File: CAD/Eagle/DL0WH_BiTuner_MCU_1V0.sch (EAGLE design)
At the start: 112 parts, among them Q0321 ABS07-32.768KHZ, U0101 STM32L476RXT_64PIN_LDO, U0521 PCAL6416APW, U2401 LM53603-Q1, U9001 TPS62051, U9401 MC33996, U9501 MC33996, U9601 MC33996, U9801 MAX232_SOIC16, U9901 MAX232_SOIC16, X2411 WIRE-TO-BOARD_5MM08_1X02, X3201 MOLEX 105017-0001, X3301 SMA_SMT_AMPHENOL-901-143, X3311 SAMTEC SMA-J-P-H-RA-TH1, X9851 WIRE-TO-BOARD_5MM08_1X02, X9852 WIRE-TO-BOARD_5MM08_1X02, X9853 WIRE-TO-BOARD_5MM08_1X02, X9951 WIRE-TO-BOARD_5MM08_1X02, X9952 WIRE-TO-BOARD_5MM08_1X02, X9953 WIRE-TO-BOARD_5MM08_1X02

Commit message: HW_1V0 - CAD/Eagle - I2C port expander not needed and removed
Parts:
- removed C0521: 100nF, df4iah_rcl:C-EUC0402
- removed R0521: 100kR, df4iah_rcl:R-EU_R0402
- removed U0521: PCAL6416APW, df4iah_dataconvertion:PCAL6416APW
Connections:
- removed net PEXPA_P0_0_R: U0521.P0_0
- removed net PEXPA_P0_1_R: U0521.P0_1
- removed net PEXPA_P0_2_R: U0521.P0_2
- removed net PEXPA_P0_3_R: U0521.P0_3
- removed net PEXPA_P0_4_R: U0521.P0_4
- removed net PEXPA_P0_5_R: U0521.P0_5
- removed net PEXPA_P0_6_R: U0521.P0_6
- removed net PEXPA_P0_7_R: U0521.P0_7
- removed net PEXPA_P1_0_R: U0521.P1_0
- removed net PEXPA_P1_1_R: U0521.P1_1
- removed net PEXPA_P1_2_R: U0521.P1_2
- removed net PEXPA_P1_3_R: U0521.P1_3
- removed net PEXPA_P1_4_R: U0521.P1_4
- removed net PEXPA_P1_5_R: U0521.P1_5
- removed net PEXPA_P1_6_R: U0521.P1_6
- removed net PEXPA_P1_7_R: U0521.P1_7
- removed net PEXPA_RESET: R0521.1, U0521.!RESET
- net +3V3: no longer C0521.1, R0521.2, U0521.VDD_I2C, U0521.VDD_P
- net GND: no longer C0521.2, U0521.ADDR, U0521.VSS
- net MCU_I2C1_SCL: no longer U0521.SCL
- net MCU_I2C1_SDA: no longer U0521.SDA
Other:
- note added: "Addr Device"
- note removed: "Addr Device 0x20/0x21 I2C Port Expander A/B 0x3D LCD access"
- note removed: "I2C1 Port Expander"
- note removed: "I2C1 Port Expander I2C1 addr: 0x20"
- note removed: "Iq=6.5uA"
- note removed: "out"
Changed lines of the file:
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@@
 <part name="GND3661" library="df4iah_supply" deviceset="GND" device=""/>
 <part name="L0411" library="df4iah_rcl" deviceset="L-EU" device="L0603" value="10uH"/>
-<part name="GND0521" library="df4iah_supply" deviceset="GND" device=""/>
-<part name="C0521" library="df4iah_rcl" deviceset="C-EU" device="C0402" value="100nF"/>
-<part name="FRAME_05" library="df4iah_frame" deviceset="A4L-LOC" device="" value="Holes"/>
-<part name="U0521" library="df4iah_dataconvertion" deviceset="PCAL6416A" device="PW"/>
-<part name="R0521" library="df4iah_rcl" deviceset="R-EU_" device="R0402" value="100kR"/>
 <part name="FRAME_24" library="df4iah_frame" deviceset="A4L-LOC" device="" value="Holes"/>
 <part name="L2411" library="df4iah_rcl" deviceset="L-EU" device="6.00X6.00MM" value="2.2uH"/>
@@
 <plain>
 <text x="134.62" y="137.16" size="2.54" layer="97" ratio="15">Addr        Device
-0x20/0x21   I2C Port Expander A/B
-0x3D        LCD access
 </text>
 <text x="22.86" y="162.56" size="2.54" layer="97" ratio="15">I2C1 Termination</text>
@@
 </segment>
 </net>
-</nets>
-</sheet>
-<sheet>
-<description>I2C1 Port Expander</description>
-<plain>
-<text x="22.86" y="162.56" size="2.54" layer="97" ratio="15">I2C1 Port Expander
-I2C1 addr: 0x20</text>
-<text x="165.1" y="15.24" size="2.54" layer="97" ratio="15">I2C1 Port Expander</text>
-<text x="106.68" y="132.08" size="1.778" layer="97">Iq=6.5uA</text>
-<text x="135.636" y="126.238" size="1.778" layer="97">out</text>
-<text x="135.636" y="121.158" size="1.778" layer="97">out</text>
-<text x="135.636" y="116.078" size="1.778" layer="97">out</text>
-<text x="135.636" y="110.998" size="1.778" layer="97">out</text>
-<text x="135.636" y="105.918" size="1.778" layer="97">out</text>
-<text x="135.636" y="100.838" size="1.778" layer="97">out</text>
-<text x="135.636" y="95.758" size="1.778" layer="97">out</text>
-<text x="135.636" y="90.678" size="1.778" layer="97">out</text>
-<text x="135.636" y="44.958" size="1.778" layer="97">out</text>
-<text x="135.636" y="50.038" size="1.778" layer="97">out</text>
-<text x="135.636" y="55.118" size="1.778" layer="97">out</text>
-<text x="135.636" y="60.198" size="1.778" layer="97">out</text>
-<text x="135.636" y="65.278" size="1.778" layer="97">out</text>
-<text x="135.636" y="70.358" size="1.778" layer="97">out</text>
-<text x="135.636" y="75.438" size="1.778" layer="97">out</text>
-<text x="135.636" y="80.518" size="1.778" layer="97">out</text>
-</plain>
-<instances>
-<instance part="FRAME_05" gate="G$1" x="0" y="0"/>
-<instance part="GND0521" gate="1" x="104.14" y="71.12"/>
-<instance part="C0521" gate="G$1" x="104.14" y="101.6"/>
-<instance part="U0521" gate="G$1" x="132.08" y="86.36"/>
-<instance part="R0521" gate="G$1" x="93.98" y="93.98" smashed="yes" rot="R90">
-<attribute name="NAME" x="92.4814" y="90.17" size="1.778" layer="95" rot="R90"/>
-<attribute name="VALUE" x="97.282" y="90.17" size="1.778" layer="96" rot="R90"/>
-</instance>
-</instances>
-<busses>
-</busses>
-<nets>
-<net name="MCU_I2C1_SCL" class="0">
-<segment>
-<wire x1="109.22" y1="66.04" x2="88.9" y2="66.04" width="0.1524" layer="91"/>
-<label x="88.9" y="66.04" size="1.778" layer="95" rot="R180" xref="yes"/>
-<pinref part="U0521" gate="G$1" pin="SCL"/>
-</segment>
-</net>
-<net name="MCU_I2C1_SDA" class="0">
-<segment>
-<wire x1="109.22" y1="60.96" x2="88.9" y2="60.96" width="0.1524" layer="91"/>
-<label x="88.9" y="60.96" size="1.778" layer="95" rot="R180" xref="yes"/>
-<pinref part="U0521" gate="G$1" pin="SDA"/>
-</segment>
-</net>
-<net name="+3V3" class="0">
-<segment>
-<wire x1="104.14" y1="104.14" x2="104.14" y2="106.68" width="0.1524" layer="91"/>
-<label x="104.14" y="134.62" size="1.778" layer="95" rot="R90" xref="yes"/>
-<pinref part="U0521" gate="G$1" pin="VDD_I2C"/>
-<wire x1="104.14" y1="106.68" x2="104.14" y2="121.92" width="0.1524" layer="91"/>
-<wire x1="104.14" y1="121.92" x2="104.14" y2="127" width="0.1524" layer="91"/>
-<wire x1="104.14" y1="127" x2="104.14" y2="134.62" width="0.1524" layer="91"/>
-<wire x1="104.14" y1="121.92" x2="109.22" y2="121.92" width="0.1524" layer="91"/>
-<junction x="104.14" y="121.92"/>
-<pinref part="U0521" gate="G$1" pin="VDD_P"/>
-<wire x1="104.14" y1="127" x2="109.22" y2="127" width="0.1524" layer="91"/>
-<junction x="104.14" y="127"/>
-<pinref part="R0521" gate="G$1" pin="2"/>
-<wire x1="93.98" y1="106.68" x2="93.98" y2="99.06" width="0.1524" layer="91"/>
-<wire x1="104.14" y1="106.68" x2="93.98" y2="106.68" width="0.1524" layer="91"/>
-<junction x="104.14" y="106.68"/>
-<pinref part="C0521" gate="G$1" pin="1"/>
-</segment>
-</net>
-<net name="PEXPA_P1_7_R" class="0">
-<segment>
-<wire x1="154.94" y1="45.72" x2="177.8" y2="45.72" width="0.1524" layer="91"/>
-<label x="177.8" y="45.72" size="1.778" layer="95" xref="yes"/>
-<pinref part="U0521" gate="G$1" pin="P1_7"/>
-</segment>
-</net>
-<net name="PEXPA_P0_1_R" class="0">
-<segment>
-<wire x1="154.94" y1="121.92" x2="177.8" y2="121.92" width="0.1524" layer="91"/>
-<label x="177.8" y="121.92" size="1.778" layer="95" xref="yes"/>
-<pinref part="U0521" gate="G$1" pin="P0_1"/>
-</segment>
-</net>
-<net name="PEXPA_P0_2_R" class="0">
-<segment>
-<wire x1="154.94" y1="116.84" x2="177.8" y2="116.84" width="0.1524" layer="91"/>
-<label x="177.8" y="116.84" size="1.778" layer="95" xref="yes"/>
-<pinref part="U0521" gate="G$1" pin="P0_2"/>
-</segment>
-</net>
-<net name="PEXPA_P0_3_R" class="0">
-<segment>
-<wire x1="154.94" y1="111.76" x2="177.8" y2="111.76" width="0.1524" layer="91"/>
-<label x="177.8" y="111.76" size="1.778" layer="95" xref="yes"/>
-<pinref part="U0521" gate="G$1" pin="P0_3"/>
-</segment>
-</net>
-<net name="PEXPA_P0_4_R" class="0">
-<segment>
-<wire x1="154.94" y1="106.68" x2="177.8" y2="106.68" width="0.1524" layer="91"/>
-<label x="177.8" y="106.68" size="1.778" layer="95" xref="yes"/>
-<pinref part="U0521" gate="G$1" pin="P0_4"/>
-</segment>
-</net>
-<net name="PEXPA_P0_5_R" class="0">
-<segment>
-<wire x1="154.94" y1="101.6" x2="177.8" y2="101.6" width="0.1524" layer="91"/>
-<label x="177.8" y="101.6" size="1.778" layer="95" xref="yes"/>
-<pinref part="U0521" gate="G$1" pin="P0_5"/>
-</segment>
-</net>
-<net name="PEXPA_P0_6_R" class="0">
-<segment>
-<wire x1="154.94" y1="96.52" x2="177.8" y2="96.52" width="0.1524" layer="91"/>
-<label x="177.8" y="96.52" size="1.778" layer="95" xref="yes"/>
-<pinref part="U0521" gate="G$1" pin="P0_6"/>
-</segment>
-</net>
-<net name="PEXPA_P0_7_R" class="0">
-<segment>
-<wire x1="154.94" y1="91.44" x2="177.8" y2="91.44" width="0.1524" layer="91"/>
-<label x="177.8" y="91.44" size="1.778" layer="95" xref="yes"/>
-<pinref part="U0521" gate="G$1" pin="P0_7"/>
-</segment>
-</net>
-<net name="PEXPA_P1_0_R" class="0">
-<segment>
-<wire x1="154.94" y1="81.28" x2="177.8" y2="81.28" width="0.1524" layer="91"/>
-<label x="177.8" y="81.28" size="1.778" layer="95" xref="yes"/>
-<pinref part="U0521" gate="G$1" pin="P1_0"/>
-</segment>
-</net>
-<net name="PEXPA_P1_1_R" class="0">
-<segment>
-<wire x1="154.94" y1="76.2" x2="177.8" y2="76.2" width="0.1524" layer="91"/>
-<label x="177.8" y="76.2" size="1.778" layer="95" xref="yes"/>
-<pinref part="U0521" gate="G$1" pin="P1_1"/>
-</segment>
-</net>
-<net name="PEXPA_P1_2_R" class="0">
-<segment>
-<wire x1="154.94" y1="71.12" x2="177.8" y2="71.12" width="0.1524" layer="91"/>
-<label x="177.8" y="71.12" size="1.778" layer="95" xref="yes"/>
-<pinref part="U0521" gate="G$1" pin="P1_2"/>
-</segment>
-</net>
-<net name="PEXPA_P1_3_R" class="0">
-<segment>
-<wire x1="154.94" y1="66.04" x2="177.8" y2="66.04" width="0.1524" layer="91"/>
-<label x="177.8" y="66.04" size="1.778" layer="95" xref="yes"/>
-<pinref part="U0521" gate="G$1" pin="P1_3"/>
-</segment>
-</net>
-<net name="PEXPA_P1_4_R" class="0">
-<segment>
-<wire x1="154.94" y1="60.96" x2="177.8" y2="60.96" width="0.1524" layer="91"/>
-<label x="177.8" y="60.96" size="1.778" layer="95" xref="yes"/>
-<pinref part="U0521" gate="G$1" pin="P1_4"/>
-</segment>
-</net>
-<net name="PEXPA_P1_5_R" class="0">
-<segment>
-<wire x1="154.94" y1="55.88" x2="177.8" y2="55.88" width="0.1524" layer="91"/>
-<label x="177.8" y="55.88" size="1.778" layer="95" xref="yes"/>
-<pinref part="U0521" gate="G$1" pin="P1_5"/>
-</segment>
-</net>
-<net name="PEXPA_P1_6_R" class="0">
-<segment>
-<wire x1="154.94" y1="50.8" x2="177.8" y2="50.8" width="0.1524" layer="91"/>
-<label x="177.8" y="50.8" size="1.778" layer="95" xref="yes"/>
-<pinref part="U0521" gate="G$1" pin="P1_6"/>
-</segment>
-</net>
-<net name="GND" class="0">
-<segment>
-<wire x1="109.22" y1="81.28" x2="104.14" y2="81.28" width="0.1524" layer="91"/>
-<wire x1="104.14" y1="81.28" x2="104.14" y2="91.44" width="0.1524" layer="91"/>
-<wire x1="104.14" y1="91.44" x2="109.22" y2="91.44" width="0.1524" layer="91"/>
-<pinref part="GND0521" gate="1" pin="GND"/>
-<wire x1="104.14" y1="73.66" x2="104.14" y2="81.28" width="0.1524" layer="91"/>
-<junction x="104.14" y="81.28"/>
-<pinref part="C0521" gate="G$1" pin="2"/>
-<wire x1="104.14" y1="91.44" x2="104.14" y2="96.52" width="0.1524" layer="91"/>
-<junction x="104.14" y="91.44"/>
-<pinref part="U0521" gate="G$1" pin="ADDR"/>
-<pinref part="U0521" gate="G$1" pin="VSS"/>
-</segment>
-</net>
-<net name="PEXPA_P0_0_R" class="0">
-<segment>
-<wire x1="154.94" y1="127" x2="177.8" y2="127" width="0.1524" layer="91"/>
-<label x="177.8" y="127" size="1.778" layer="95" xref="yes"/>
-<pinref part="U0521" gate="G$1" pin="P0_0"/>
-</segment>
-</net>
-<net name="PEXPA_RESET" class="0">
-<segment>
-<pinref part="R0521" gate="G$1" pin="1"/>
-<wire x1="93.98" y1="88.9" x2="93.98" y2="76.2" width="0.1524" layer="91"/>
-<wire x1="93.98" y1="76.2" x2="109.22" y2="76.2" width="0.1524" layer="91"/>
-<pinref part="U0521" gate="G$1" pin="!RESET"/>
-</segment>
-</net>

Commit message: HW_1V0 - CAD/Eagle - I2C port added
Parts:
- added C8901, C8902: 10nF, df4iah_rcl:C-EUC0603
- added C8911: (no value), df4iah_rcl:C-EUC0603
- added C8921: 100nF, df4iah_rcl:C-EUC0603
- added D8921, D8922: CMAD6001, df4iah_diode:D_SOD923
- added L8901, L8902: 10uH, df4iah_rcl:L-EUL0603
- added R8901, R8902: 1kR, df4iah_rcl:R-EU_R0603
- added R8903, R8904, R8923: 10kR, df4iah_rcl:R-EU_R0603
- added R8911, R8912, R8922: 47R, df4iah_rcl:R-EU_R0603
- added R8921: 1MR, df4iah_rcl:R-EU_R0603
- added U8911: TS5A23166, df4iah_sc-switches:TS5A23166
- added U8921: OPA354, df4iah_opamp:OPA354
- added X0601: (no value), df4iah_connector:HEADER-2X2
- L9011: device df4iah_rcl:L-EU8.00X8.00MM -> df4iah_rcl:L-EUL0603
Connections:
- removed net MCU_I2C1_SCL: R0612.1
- removed net MCU_I2C1_SDA: R0611.1
- removed net N$1: R9901.1
- removed net N$10: R9621.1
- removed net N$11: R9622.1
- removed net N$14: R9623.1
- removed net N$16: R9624.1
- removed net N$17: R9625.1
- removed net N$18: R9626.1
- removed net N$3: R9902.1
- removed net N$30: R9524.1
- removed net N$31: R9424.1
- removed net N$4: R9903.1
- removed net N$5: R9904.1
- removed net N$6: R9801.1
- removed net N$7: R9802.1
- removed net N$8: R9803.1
- removed net N$9: R9804.1
- removed net PA12PA11_N: X3201.J_D-
- removed net PA12PA11_P: X3201.J_D+
- removed net RM_BCK: X3311.1
- new net RM_REV: L8902.2, X3311.1
- new net SWR_IN_FWD: R8902.2, R8904.2, U8911.1
- new net SWR_IN_FWD_HI: C8901.1, L8901.1, R8904.1
- new net SWR_IN_REV: R8901.2, R8903.2, U8911.5
- new net SWR_IN_REV_HI: C8902.1, L8902.1, R8903.1
- new net SWR_OP_M: D8921.A, R8921.2, U8921.-IN
- new net SWR_OP_OUT: D8921.C, R8922.1, U8921.OUT
- new net SWR_SEL_FWD: R8911.2, U8911.7
- new net SWR_SEL_PWR: R8921.1, U8911.2, U8911.6
- new net SWR_SEL_REV: R8912.2, U8911.3
- net +3V3: now also C8911.1, C8921.1, R8923.1, U8911.8, U8921.V+
- net GND: now also C8901.2, C8902.2, C8911.2, C8921.2, D8922.C, R8901.1, R8902.1, U8911.4, U8921.+IN, U8921.V-, X0601.2, X0601.4
- net PA0: now also R9901.1
- net PA1: now also R9902.1
- net PA11: now also X3201.J_D-
- net PA12: now also X3201.J_D+
- net PA15: now also R9903.1
- net PA3: now also R8912.1
- net PA5: now also R9621.1
- net PA6: now also R9622.1
- net PA7: now also R9623.1
- net PB0: now also R9624.1
- net PB1: now also R9524.1
- net PB10: now also R9802.1
- net PB11: now also R9626.1
- net PB12: now also R9803.1
- net PB13: now also R9804.1
- net PB2: now also R9424.1
- net PB6: now also R0612.1, X0601.1
- net PB7: now also R9904.1
- net PB9: now also R0611.1, X0601.3
- net PC0: now also R8922.2
- net PC1: now also R9801.1
- net PC2: now also D8922.A, R8923.2
- net PC3: now also R8911.1
- net PC4: now also R9625.1
- net RM_FWD: now also L8901.2
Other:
- note added: "Logarithmic Amp"
- note added: "MCU_I2C1_SCL"
- note added: "MCU_I2C1_SDA"
- note added: "PMIC 12V --> 5V0"
- note added: "SMA direct. coupler FWD"
- note added: "SMA direct. coupler REV"
- note added: "SWR metering"
- note added: "SWR_ADC"
- note added: "SWR_TEMP"
- note added: "Switch"
- note added: "WE PD 744 777 10 8.00mm x 8.00mm"
- note removed: "12V Down-Converter --> 5V0"
- note removed: "SMA direct. coupler backward"
- note removed: "SMA direct. coupler forward"

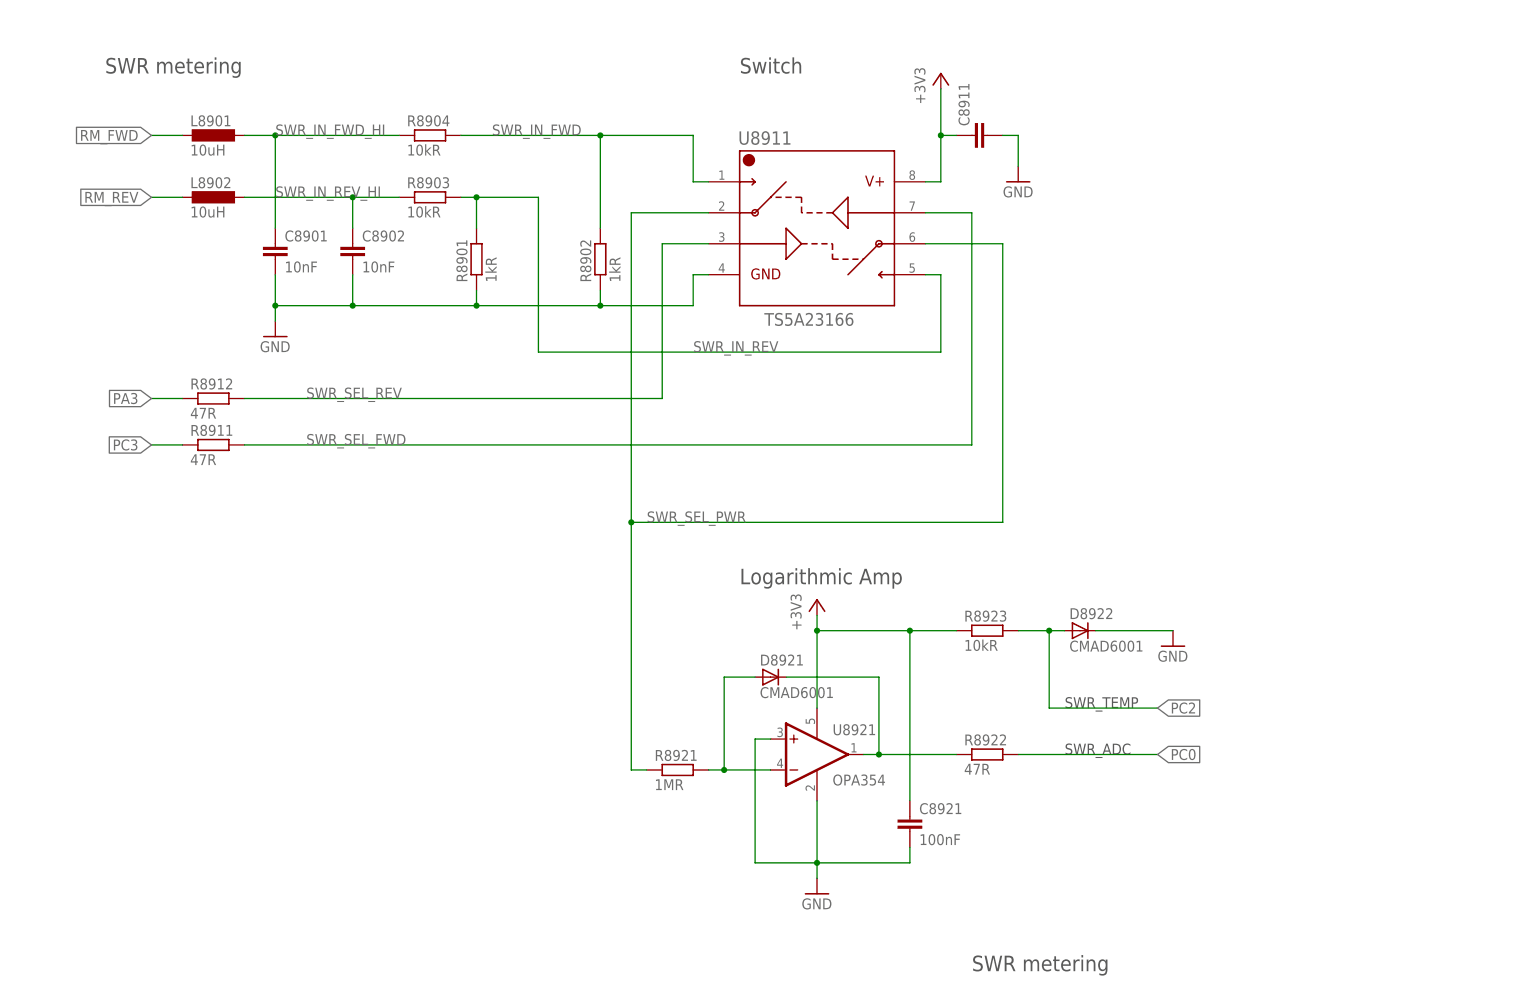
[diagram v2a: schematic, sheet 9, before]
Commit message: HW_1V0 - CAD/Eagle - SWR metering added, all placed
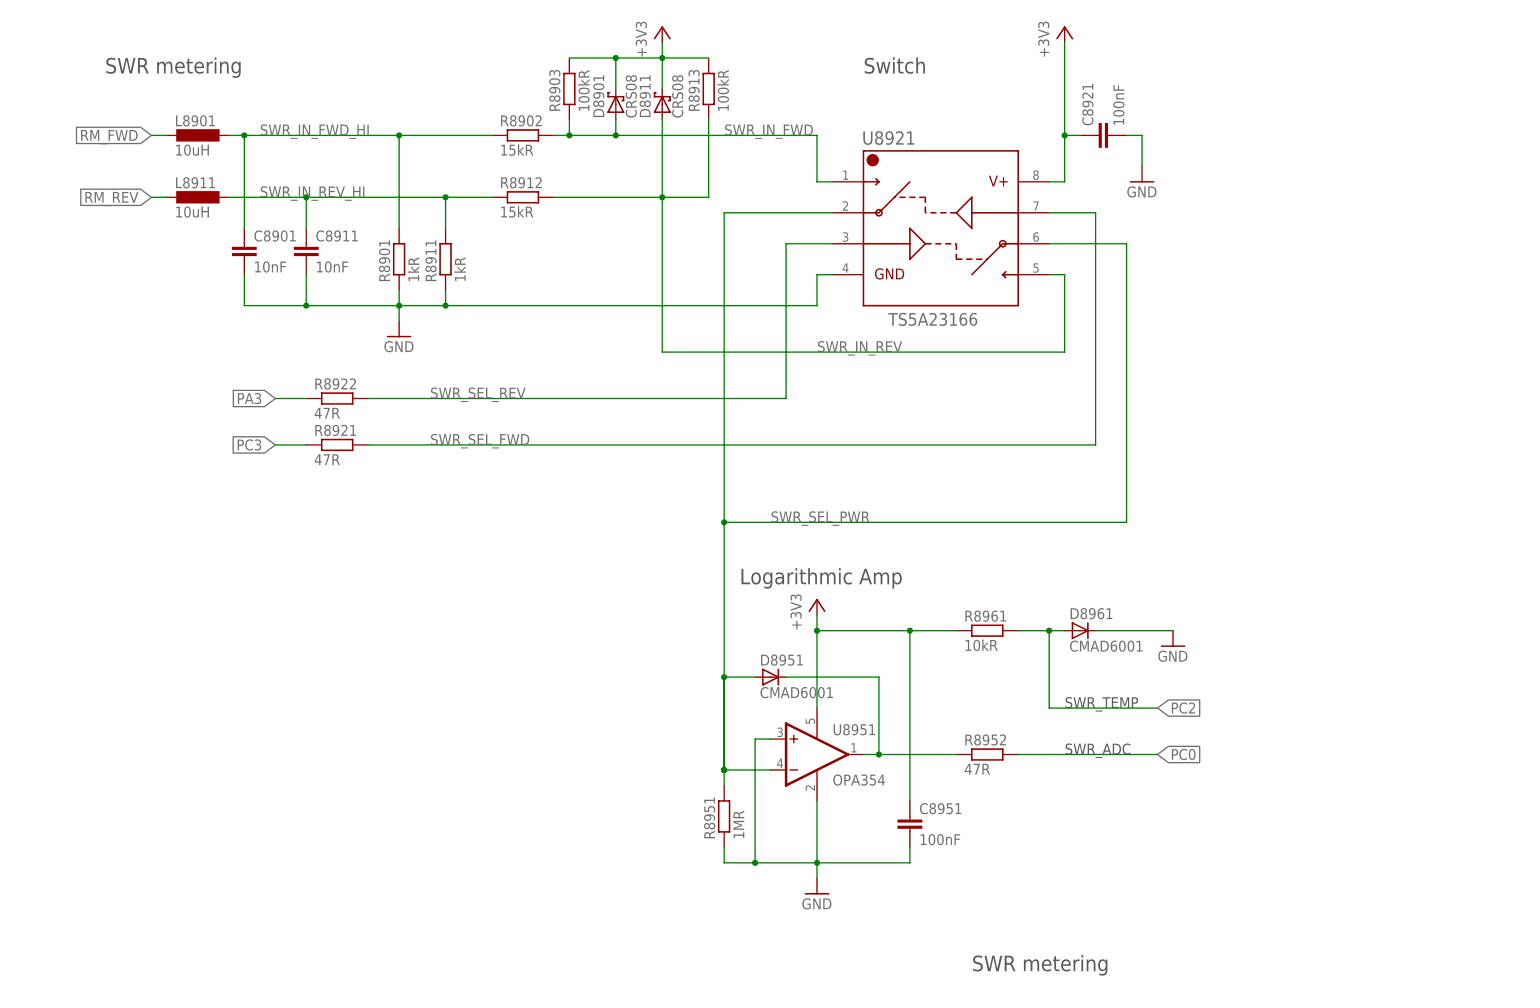
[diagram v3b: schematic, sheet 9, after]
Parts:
- removed C8902: 10nF, df4iah_rcl:C-EUC0603
- removed L8902: 10uH, df4iah_rcl:L-EUL0603
- removed R8904: 10kR, df4iah_rcl:R-EU_R0603
- removed U8911: TS5A23166, df4iah_sc-switches:TS5A23166
- added C8951: 100nF, df4iah_rcl:C-EUC0603
- added D8901, D8911: CRS08, df4iah_diode:CRS08
- added L8911: 10uH, df4iah_rcl:L-EUL0603
- added R8913: 100kR, df4iah_rcl:R-EU_R0603
- added R8951: 1MR, df4iah_rcl:R-EU_R0603
- added R8952: 47R, df4iah_rcl:R-EU_R0603
- added U8951: OPA354, df4iah_opamp:OPA354
- C8911: value (none) -> 10nF
- R8902: value 1kR -> 15kR
- R8903: value 10kR -> 100kR
- R8911: value 47R -> 1kR
- R8912: value 47R -> 15kR
- R8921: value 1MR -> 47R
- U8921: value OPA354 -> TS5A23166; device df4iah_opamp:OPA354 -> df4iah_sc-switches:TS5A23166
- renumbered D8921 to D8951, D8922 to D8961, R8923 to R8961
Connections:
- removed net SWR_OP_M: D8951.A, R8921.2, U8921.-IN
- net +3V3: now also C8951.1, D8901.C, D8911.C, R8903.2, R8913.2, U8921.8, U8951.V+; no longer C8911.1, U8911.8, U8921.V+
- net GND: now also C8951.2, R8911.1, R8951.1, U8921.4, U8951.+IN, U8951.V-; no longer C8902.2, R8902.1, U8911.4, U8921.+IN, U8921.V-
- net PA3: now also R8922.1; no longer R8912.1
- net PC0: now also R8952.2; no longer R8922.2
- net PC3: now also R8921.1; no longer R8911.1
- net RM_REV: now also L8911.2; no longer L8902.2
- net SWR_IN_FWD: now also D8901.A, R8903.1, U8921.1; no longer R8904.2, U8911.1
- net SWR_IN_FWD_HI: now also R8901.2, R8902.1; no longer R8904.1
- net SWR_IN_REV: now also D8911.A, R8912.2, R8913.1, U8921.5; no longer R8901.2, R8903.2, U8911.5
- net SWR_IN_REV_HI: now also C8911.1, L8911.1, R8911.2, R8912.1; no longer C8902.1, L8902.1, R8903.1
- net SWR_OP_OUT: now also R8952.1, U8951.OUT; no longer R8922.1, U8921.OUT
- net SWR_SEL_FWD: now also R8921.2, U8921.7; no longer R8911.2, U8911.7
- net SWR_SEL_PWR: now also D8951.A, R8951.2, U8921.2, U8921.6, U8951.-IN; no longer R8921.1, U8911.2, U8911.6
- net SWR_SEL_REV: now also R8922.2, U8921.3; no longer R8912.2, U8911.3
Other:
- moved on the sheet: C8901, C8911, C8921, L8901, R8901, R8902, R8903, R8911, R8912, R8921, R8922
